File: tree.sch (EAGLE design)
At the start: 31 parts, among them J1 M03X2-NOSILK, J2 CON_TERMINAL_HOLES, U2 MCP1702-5

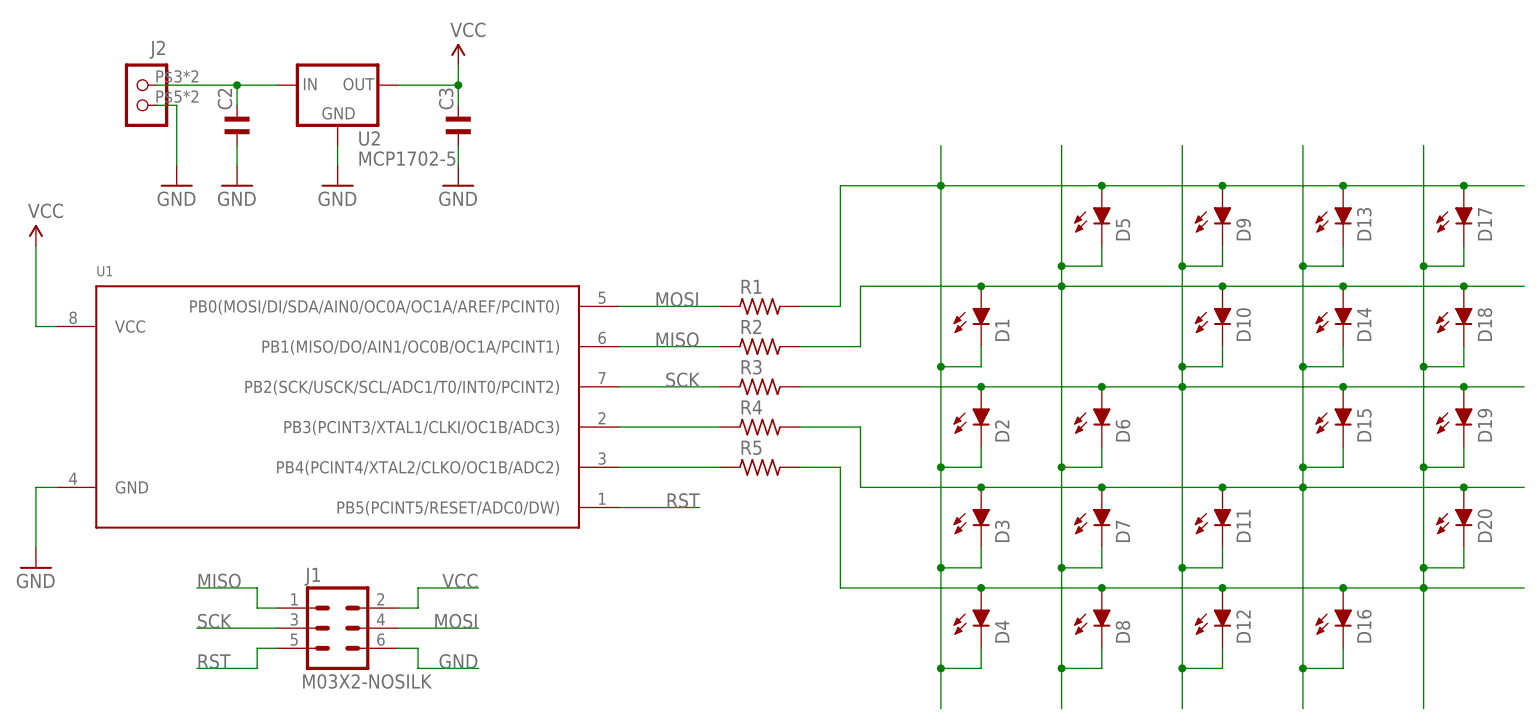
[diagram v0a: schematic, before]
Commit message: Created png. Added values to schematic.
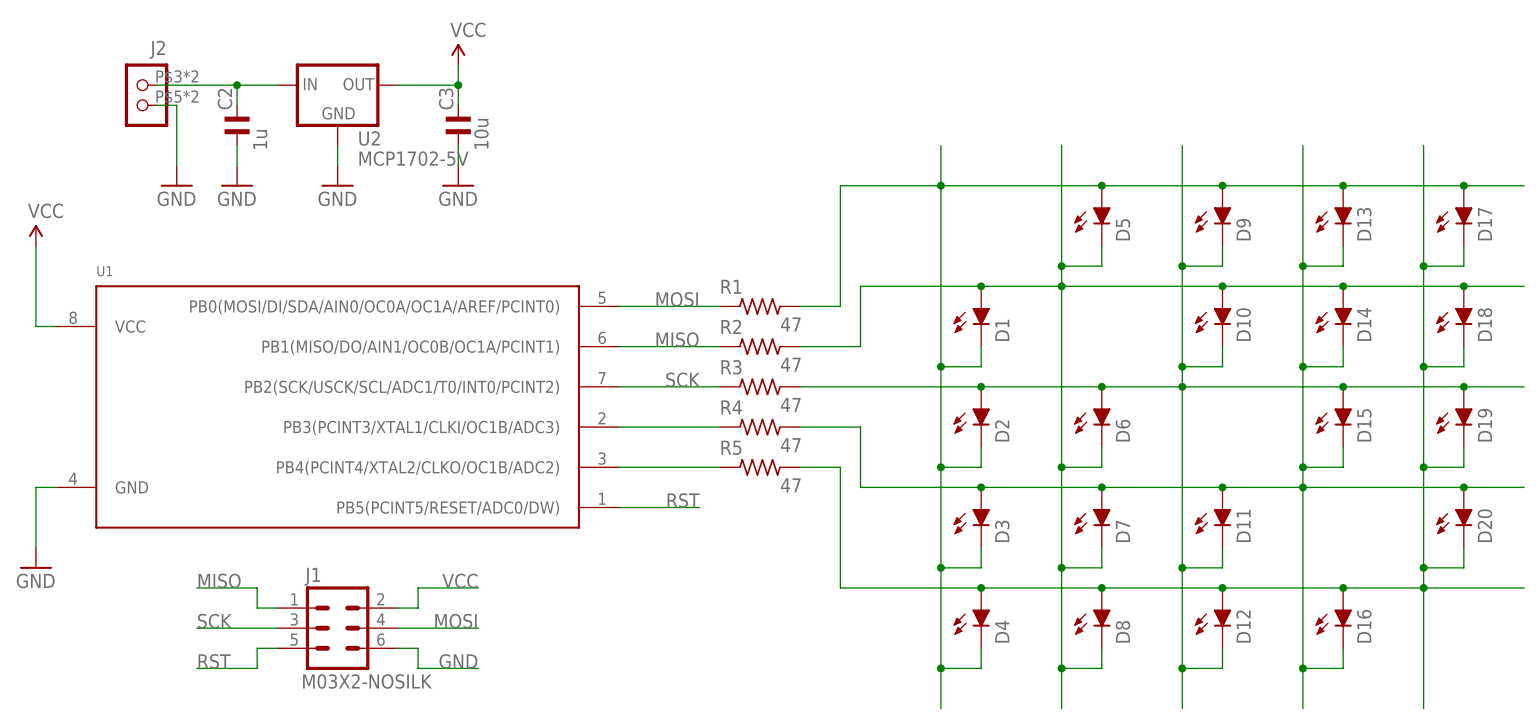
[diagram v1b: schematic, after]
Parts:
- C2: value (none) -> 1u
- C3: value (none) -> 10u
- R1, R2, R3, R4, R5: value (none) -> 47
- U2: value MCP1702-5 -> MCP1702-5V
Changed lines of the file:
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@@
 <layer number="91" name="Nets" color="2" fill="1" visible="yes" active="yes"/>
 <layer number="92" name="Busses" color="1" fill="1" visible="yes" active="yes"/>
-<layer number="93" name="Pins" color="2" fill="1" visible="yes" active="yes"/>
+<layer number="93" name="Pins" color="2" fill="1" visible="no" active="yes"/>
 <layer number="94" name="Symbols" color="4" fill="1" visible="yes" active="yes"/>
 <layer number="95" name="Names" color="7" fill="1" visible="yes" active="yes"/>
@@
 <parts>
 <part name="U1" library="snowflake" deviceset="ATTINY*5" device="-20SU-NOSILK"/>
-<part name="R1" library="snowflake" deviceset="R_" device="0805NOSILK"/>
-<part name="R2" library="snowflake" deviceset="R_" device="0805NOSILK"/>
-<part name="R3" library="snowflake" deviceset="R_" device="0805NOSILK"/>
-<part name="R4" library="snowflake" deviceset="R_" device="0805NOSILK"/>
-<part name="R5" library="snowflake" deviceset="R_" device="0805NOSILK"/>
+<part name="R1" library="snowflake" deviceset="R_" device="0805NOSILK" value="47"/>
+<part name="R2" library="snowflake" deviceset="R_" device="0805NOSILK" value="47"/>
+<part name="R3" library="snowflake" deviceset="R_" device="0805NOSILK" value="47"/>
+<part name="R4" library="snowflake" deviceset="R_" device="0805NOSILK" value="47"/>
+<part name="R5" library="snowflake" deviceset="R_" device="0805NOSILK" value="47"/>
 <part name="SUPPLY1" library="SparkFun-Aesthetics" deviceset="VCC" device=""/>
 <part name="GND1" library="SparkFun-Aesthetics" deviceset="GND" device=""/>
@@
 <part name="D20" library="snowflake" deviceset="LED" device="CHIP-LED0805NOSILK"/>
 <part name="J1" library="snowflake" deviceset="M03X2" device="-NOSILK"/>
-<part name="C2" library="snowflake" deviceset="C_" device="0805NOSILK"/>
-<part name="C3" library="snowflake" deviceset="C_" device="0805NOSILK"/>
+<part name="C2" library="snowflake" deviceset="C_" device="0805NOSILK" value="1u"/>
+<part name="C3" library="snowflake" deviceset="C_" device="0805NOSILK" value="10u"/>
 <part name="GND2" library="SparkFun-Aesthetics" deviceset="GND" device=""/>
 <part name="GND3" library="SparkFun-Aesthetics" deviceset="GND" device=""/>
@@
 <part name="SUPPLY2" library="SparkFun-Aesthetics" deviceset="VCC" device=""/>
 <part name="GND5" library="SparkFun-Aesthetics" deviceset="GND" device=""/>
-<part name="U2" library="snowflake" deviceset="V_REG_MCP170X" device="-CB-NOSILK" value="MCP1702-5"/>
+<part name="U2" library="snowflake" deviceset="V_REG_MCP170X" device="-CB-NOSILK" value="MCP1702-5V"/>
 <part name="J2" library="adi-misc" deviceset="CON_TERMINAL_HOLES" device=""/>
 </parts>
@@
 <instances>
 <instance part="U1" gate="G$1" x="40.64" y="43.18"/>
-<instance part="R1" gate="G$1" x="93.98" y="55.88"/>
-<instance part="R2" gate="G$1" x="93.98" y="50.8"/>
-<instance part="R3" gate="G$1" x="93.98" y="45.72"/>
-<instance part="R4" gate="G$1" x="93.98" y="40.64"/>
-<instance part="R5" gate="G$1" x="93.98" y="35.56"/>
+<instance part="R1" gate="G$1" x="93.98" y="55.88" smashed="yes">
+<attribute name="NAME" x="88.9" y="57.4675" size="1.778" layer="95"/>
+<attribute name="VALUE" x="96.52" y="52.705" size="1.778" layer="96"/>
+</instance>
+<instance part="R2" gate="G$1" x="93.98" y="50.8" smashed="yes">
+<attribute name="NAME" x="88.9" y="52.3875" size="1.778" layer="95"/>
+<attribute name="VALUE" x="96.52" y="47.625" size="1.778" layer="96"/>
+</instance>
+<instance part="R3" gate="G$1" x="93.98" y="45.72" smashed="yes">
+<attribute name="NAME" x="88.9" y="47.3075" size="1.778" layer="95"/>
+<attribute name="VALUE" x="96.52" y="42.545" size="1.778" layer="96"/>
+</instance>
+<instance part="R4" gate="G$1" x="93.98" y="40.64" smashed="yes">
+<attribute name="NAME" x="88.9" y="42.2275" size="1.778" layer="95"/>
+<attribute name="VALUE" x="96.52" y="37.465" size="1.778" layer="96"/>
+</instance>
+<instance part="R5" gate="G$1" x="93.98" y="35.56" smashed="yes">
+<attribute name="NAME" x="88.9" y="37.1475" size="1.778" layer="95"/>
+<attribute name="VALUE" x="96.52" y="32.385" size="1.778" layer="96"/>
+</instance>
 <instance part="SUPPLY1" gate="G$1" x="2.54" y="63.5"/>
 <instance part="GND1" gate="1" x="2.54" y="22.86"/>
